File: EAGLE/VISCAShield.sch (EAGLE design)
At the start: 35 parts, among them J1 RJHSE-5381

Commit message: Some revisions.
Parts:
- added C1, C2, C3, C4, C5: 1.0uF, SparkFun-Capacitors:1.0UF-0805-25V-(+80/-20%)
- added U1: MAX3232, SparkFun-IC-Comms:MAX2323SOIC16
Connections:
- new net 232RX: J1.6, U1.R1IN
- new net 232TX: J1.3, U1.T1OUT
- new net C1+: C1.1, U1.C1+
- new net C1-: C1.2, U1.C1-
- new net C2+: C2.1, U1.C2+
- new net C2-: C2.2, U1.C2-
- new net RS232V+: C3.1, U1.V+
- new net RS232V-: C4.1, U1.V-
- net 5V: now also C5.1, U1.VCC
- net GND: now also C3.2, C4.2, C5.2, U1.GND, U1.R2IN, U1.T2IN
- net RX: now also U1.R1OUT; no longer J1.6
- net TX: now also U1.T1IN; no longer J1.3

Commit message: Add optional AREF input jumper.  Clean up unused nets from schematic.
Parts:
- added AREF: 0ohm, BeagleBone_Black_Wireless:R-US_0204/2V
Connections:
- new net AREF: AREF.1, B1.AREF
- net 5V: now also AREF.2
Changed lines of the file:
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@@
 <part name="C4" library="SparkFun-Capacitors" library_urn="urn:adsk.eagle:library:510" deviceset="1.0UF" device="-0805-25V-(+80/-20%)" package3d_urn="urn:adsk.eagle:package:37429/1" value="1.0uF"/>
 <part name="C5" library="SparkFun-Capacitors" library_urn="urn:adsk.eagle:library:510" deviceset="1.0UF" device="-0805-25V-(+80/-20%)" package3d_urn="urn:adsk.eagle:package:37429/1" value="1.0uF"/>
+<part name="AREF" library="BeagleBone_Black_Wireless" library_urn="urn:adsk.eagle:library:6644236" deviceset="R-US_" device="0204/2V" package3d_urn="urn:adsk.eagle:package:8118463/1" value="0ohm"/>
 </parts>
 <sheets>
@@
 <attribute name="NAME" x="85.344" y="30.861" size="1.778" layer="95" font="vector"/>
 <attribute name="VALUE" x="85.344" y="25.781" size="1.778" layer="96" font="vector"/>
+</instance>
+<instance part="AREF" gate="G$1" x="111.76" y="101.6" smashed="yes">
+<attribute name="NAME" x="107.95" y="103.0986" size="1.778" layer="95"/>
+<attribute name="VALUE" x="107.95" y="98.298" size="1.778" layer="96"/>
 </instance>
 </instances>
@@
 <label x="83.82" y="40.64" size="1.778" layer="95"/>
 </segment>
+<segment>
+<pinref part="AREF" gate="G$1" pin="2"/>
+<wire x1="116.84" y1="101.6" x2="127" y2="101.6" width="0.1524" layer="91"/>
+<label x="121.92" y="101.6" size="1.778" layer="95"/>
+</segment>
 </net>
 <net name="PAN" class="0">
@@
 </segment>
 </net>
+<net name="AREF" class="0">
+<segment>
+<pinref part="B1" gate="G$1" pin="AREF"/>
+<wire x1="27.94" y1="-12.7" x2="12.7" y2="-12.7" width="0.1524" layer="91"/>
+<label x="12.7" y="-12.7" size="1.778" layer="95"/>
+</segment>
+<segment>
+<pinref part="AREF" gate="G$1" pin="1"/>
+<wire x1="106.68" y1="101.6" x2="96.52" y2="101.6" width="0.1524" layer="91"/>
+<label x="96.52" y="101.6" size="1.778" layer="95"/>
+</segment>
+</net>

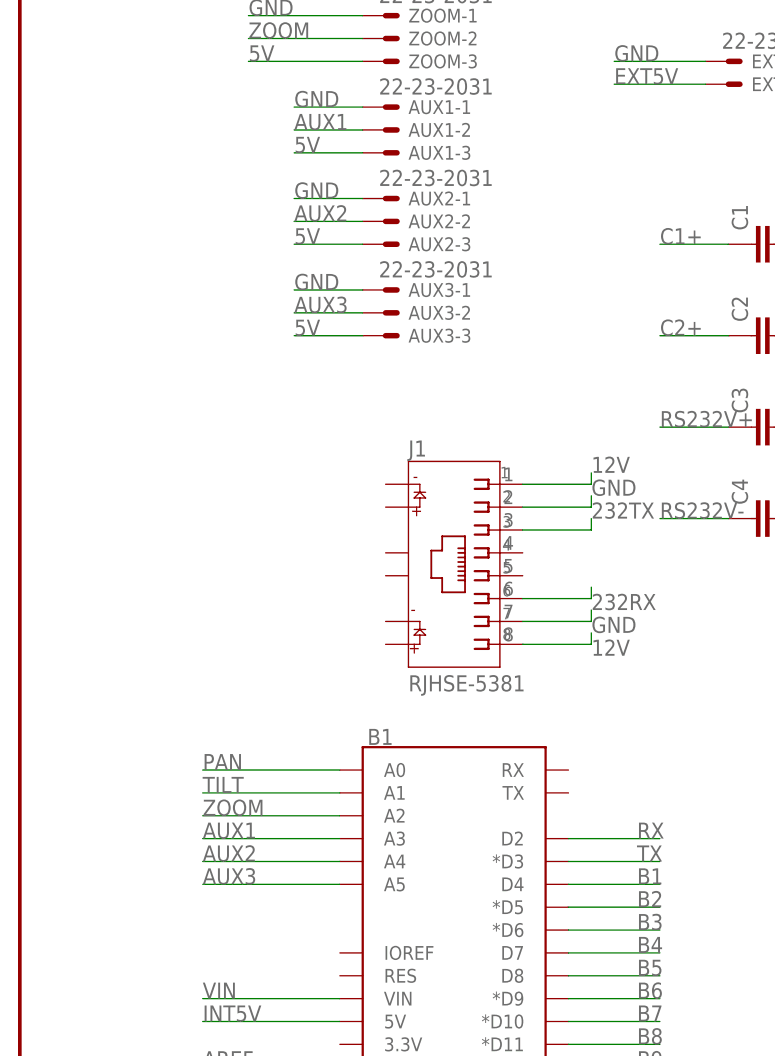
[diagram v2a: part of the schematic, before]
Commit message: Successful build of Visca shield & more testing of control code.
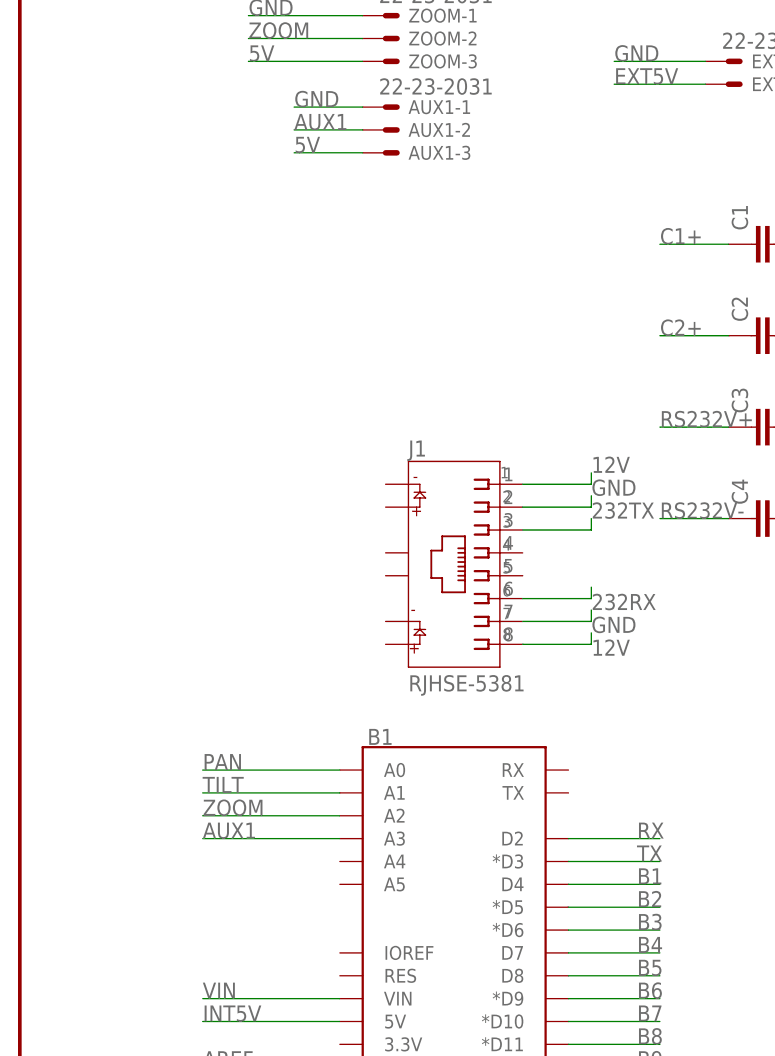
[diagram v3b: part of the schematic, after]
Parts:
- removed AUX2, AUX3: 22-23-2031, con-molex:22-23-2031
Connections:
- removed net AUX2: AUX2-2.S, B1.A4
- removed net AUX3: AUX3-2.S, B1.A5
- net 5V: no longer AUX2-3.S, AUX3-3.S
- net GND: no longer AUX2-1.S, AUX3-1.S
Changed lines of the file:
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@@
 <part name="R10" library="BeagleBone_Black_Wireless" library_urn="urn:adsk.eagle:library:6644236" deviceset="R-US_" device="0204/2V" package3d_urn="urn:adsk.eagle:package:8118463/1" value="10kohm"/>
 <part name="AUX1" library="con-molex" library_urn="urn:adsk.eagle:library:165" deviceset="22-23-2031" device="" package3d_urn="urn:adsk.eagle:package:8078634/1"/>
-<part name="AUX2" library="con-molex" library_urn="urn:adsk.eagle:library:165" deviceset="22-23-2031" device="" package3d_urn="urn:adsk.eagle:package:8078634/1"/>
-<part name="AUX3" library="con-molex" library_urn="urn:adsk.eagle:library:165" deviceset="22-23-2031" device="" package3d_urn="urn:adsk.eagle:package:8078634/1"/>
 <part name="I2C" library="con-molex" library_urn="urn:adsk.eagle:library:165" deviceset="22-23-2041" device="" package3d_urn="urn:adsk.eagle:package:8078635/1"/>
 <part name="EXT5V" library="con-molex" library_urn="urn:adsk.eagle:library:165" deviceset="22-23-2021" device="" package3d_urn="urn:adsk.eagle:package:8078633/1"/>
@@
 <attribute name="NAME" x="35.56" y="88.138" size="1.524" layer="95"/>
 </instance>
-<instance part="AUX2" gate="-1" x="33.02" y="83.82" smashed="yes">
-<attribute name="NAME" x="35.56" y="83.058" size="1.524" layer="95"/>
-<attribute name="VALUE" x="32.258" y="85.217" size="1.778" layer="96"/>
-</instance>
-<instance part="AUX2" gate="-2" x="33.02" y="81.28" smashed="yes">
-<attribute name="NAME" x="35.56" y="80.518" size="1.524" layer="95"/>
-</instance>
-<instance part="AUX2" gate="-3" x="33.02" y="78.74" smashed="yes">
-<attribute name="NAME" x="35.56" y="77.978" size="1.524" layer="95"/>
-</instance>
-<instance part="AUX3" gate="-1" x="33.02" y="73.66" smashed="yes">
-<attribute name="NAME" x="35.56" y="72.898" size="1.524" layer="95"/>
-<attribute name="VALUE" x="32.258" y="75.057" size="1.778" layer="96"/>
-</instance>
-<instance part="AUX3" gate="-2" x="33.02" y="71.12" smashed="yes">
-<attribute name="NAME" x="35.56" y="70.358" size="1.524" layer="95"/>
-</instance>
-<instance part="AUX3" gate="-3" x="33.02" y="68.58" smashed="yes">
-<attribute name="NAME" x="35.56" y="67.818" size="1.524" layer="95"/>
-</instance>
 <instance part="I2C" gate="-1" x="71.12" y="124.46" smashed="yes">
 <attribute name="NAME" x="73.66" y="123.698" size="1.524" layer="95"/>
@@
 </segment>
 <segment>
-<pinref part="AUX2" gate="-1" pin="S"/>
-<wire x1="30.48" y1="83.82" x2="22.86" y2="83.82" width="0.1524" layer="91"/>
-<label x="22.86" y="83.82" size="1.778" layer="95"/>
-</segment>
-<segment>
-<pinref part="AUX3" gate="-1" pin="S"/>
-<wire x1="30.48" y1="73.66" x2="22.86" y2="73.66" width="0.1524" layer="91"/>
-<label x="22.86" y="73.66" size="1.778" layer="95"/>
-</segment>
-<segment>
 <pinref part="EXT5V" gate="-1" pin="S"/>
 <wire x1="68.58" y1="99.06" x2="58.42" y2="99.06" width="0.1524" layer="91"/>
@@
 <wire x1="30.48" y1="88.9" x2="22.86" y2="88.9" width="0.1524" layer="91"/>
 <label x="22.86" y="88.9" size="1.778" layer="95"/>
-</segment>
-<segment>
-<pinref part="AUX2" gate="-3" pin="S"/>
-<wire x1="30.48" y1="78.74" x2="22.86" y2="78.74" width="0.1524" layer="91"/>
-<label x="22.86" y="78.74" size="1.778" layer="95"/>
-</segment>
-<segment>
-<pinref part="AUX3" gate="-3" pin="S"/>
-<wire x1="30.48" y1="68.58" x2="22.86" y2="68.58" width="0.1524" layer="91"/>
-<label x="22.86" y="68.58" size="1.778" layer="95"/>
 </segment>
 <segment>
@@
 </segment>
 </net>
-<net name="AUX2" class="0">
-<segment>
-<pinref part="B1" gate="G$1" pin="A4"/>
-<wire x1="27.94" y1="10.16" x2="12.7" y2="10.16" width="0.1524" layer="91"/>
-<label x="12.7" y="10.16" size="1.778" layer="95"/>
-</segment>
-<segment>
-<pinref part="AUX2" gate="-2" pin="S"/>
-<wire x1="30.48" y1="81.28" x2="22.86" y2="81.28" width="0.1524" layer="91"/>
-<label x="22.86" y="81.28" size="1.778" layer="95"/>
-</segment>
-</net>
-<net name="AUX3" class="0">
-<segment>
-<pinref part="B1" gate="G$1" pin="A5"/>
-<wire x1="27.94" y1="7.62" x2="12.7" y2="7.62" width="0.1524" layer="91"/>
-<label x="12.7" y="7.62" size="1.778" layer="95"/>
-</segment>
-<segment>
-<pinref part="AUX3" gate="-2" pin="S"/>
-<wire x1="30.48" y1="71.12" x2="22.86" y2="71.12" width="0.1524" layer="91"/>
-<label x="22.86" y="71.12" size="1.778" layer="95"/>
-</segment>
-</net>
